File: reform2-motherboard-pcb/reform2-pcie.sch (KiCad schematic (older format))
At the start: 48 parts, among them J10 1-2199230-6, J11 48099-5701, Q14 PMV50EPEAR, U11 679105700, U23 IDT5V41066, Y3 25MHz

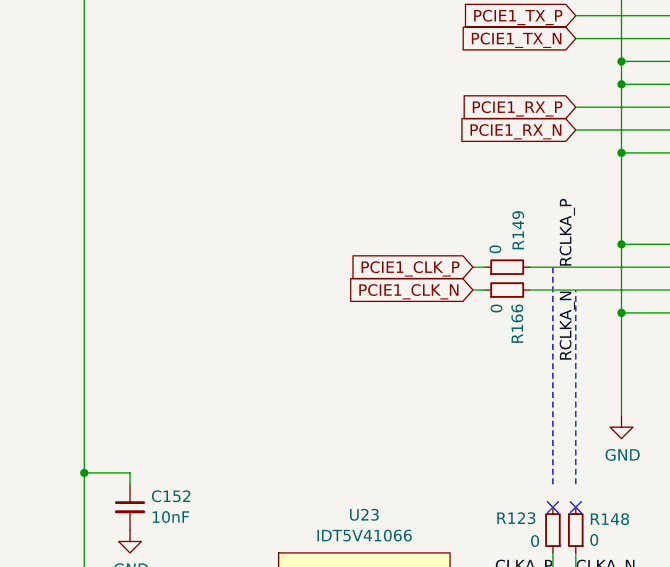
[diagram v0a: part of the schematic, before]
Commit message: WIP license clarification, motherboard now CERN-OHL-S 2.0
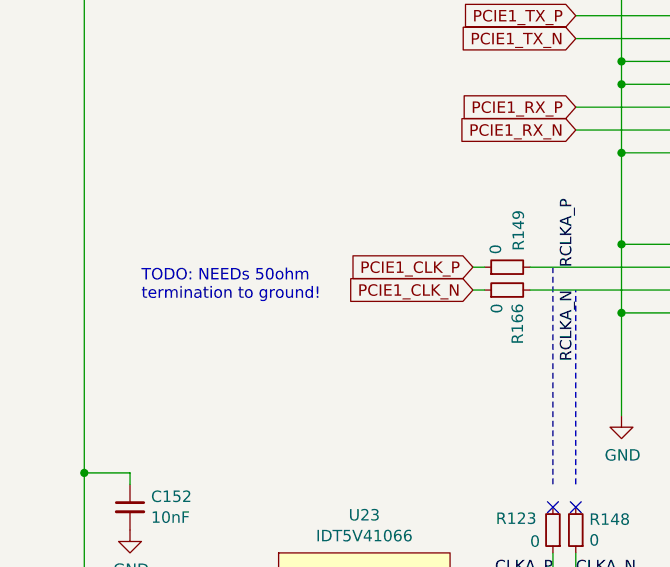
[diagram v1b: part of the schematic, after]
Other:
- note added: "TODO: NEEDs 50ohm\ntermination to ground!"
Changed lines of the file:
@@
 EESchema Schematic File Version 4
-LIBS:reform2-motherboard-cache
-EELAYER 29 0
+EELAYER 30 0
 EELAYER END
 $Descr A4 11693 8268
@@
 Sheet 5 9
 Title "MNT Reform 2 PCIe"
-Date "2020-02-07"
-Rev "2.0D-3"
+Date "2020-04-11"
+Rev "2.0D-4"
 Comp "MNT Research GmbH"
 Comment1 "https://mntre.com"
 Comment2 "Engineer: Lukas F. Hartmann"
-Comment3 "License: GPL v3+"
+Comment3 "License: CERN-OHL-S 2.0"
 Comment4 ""
 $EndDescr
@@
 $EndComp
 Connection ~ 7050 1800
-$Bitmap
-Pos 10600 6850
-Scale 1.000000
-Data
-89 50 4E 47 0D 0A 1A 0A 00 00 00 0D 49 48 44 52 00 00 01 2C 00 00 00 70 08 06 00 00 00 A4 46 4D
-4D 00 00 00 04 73 42 49 54 08 08 08 08 7C 08 64 88 00 00 06 2D 49 44 41 54 78 9C ED DD BB 8B 1D
-65 1C 87 F1 67 77 45 B1 08 82 26 F1 D2 6A 5A FF 00 0B B5 16 4C 36 12 5D 2F 9D 69 BC 04 0D 5E 62
-A3 A4 B1 D0 CE 4B C4 24 42 2A 05 03 21 85 FA 07 68 B4 8A 60 67 21 12 6D 04 0D 1A 90 04 4C 97 B5
-98 19 CE 64 F7 9C 39 B7 77 DE DF 7B F6 3C 1F 38 EC 16 CB EC 97 2D 1E 66 66 77 CF 80 24 49 92 24
-49 92 24 49 92 24 49 92 24 49 92 24 49 92 24 49 92 24 49 92 24 49 92 24 49 52 42 8F 00 7B A2 47
-B4 1C 8A 1E D0 F2 10 70 5F F4 08 49 03 C7 81 B3 94 13 AD 3F 80 67 A2 47 D4 8E 02 DF 60 B4 A4 62
-1C 07 36 29 27 5A D7 81 7F 28 23 5A 47 A9 7E 36 5F 63 B4 A4 22 34 C1 2A 25 5A D7 EB 2D 25 44 AB
-09 96 D1 92 0A D1 0E 56 09 D1 6A 82 55 42 B4 DA C1 32 5A 52 01 B6 06 AB 89 D6 EE A0 3D ED 60 45
-47 6B 6B B0 8C 96 14 6C 58 B0 22 A3 B5 35 58 91 D1 1A 16 2C A3 25 05 1A 15 AC A8 68 0D 0B 56 54
-B4 46 05 AB 89 D6 BD 99 F7 48 4B AF 2B 58 11 D1 1A 15 AC 88 68 75 05 6B 13 F8 0A A3 25 65 35 2E
-58 B9 A3 D5 15 AC 4D E0 6F F2 45 6B 5C B0 8C 96 94 D9 24 C1 DA 04 BE 24 4F B4 C6 05 2B 67 B4 26
-09 96 D1 92 32 9A 34 58 B9 A2 35 49 B0 9A 68 3D DD F3 96 49 83 65 B4 34 97 5B A2 07 EC 50 1B F5
-C7 23 54 F7 93 22 ED 06 3E 66 70 C9 1A ED 71 AA 2D 2F 00 7F F6 F4 3D 1E 05 6E ED E9 D8 7D B8 54
-BF 34 86 C1 EA 4F 69 D1 3A 51 7F 5E 42 B4 F6 D7 1F FB 8A D6 67 C4 FF 27 C2 34 DE AB 5F 1A C3 60
-F5 CB 68 8D D6 67 B4 76 01 77 24 3E 66 9F 6E 8B 1E B0 28 56 A3 07 2C 81 0D AA 50 44 FD 45 7C 5B
-13 AD 8D 71 5F 98 C9 7E E0 24 DE D3 D2 84 0C 56 1E 1B 54 F7 91 EE 8A 1E C2 E0 9E 96 D1 D2 C2 31
-58 F9 94 14 AD 3D 18 2D 2D 20 83 95 CF 0A D5 9F 17 18 AD E1 8C 96 C6 32 58 79 95 1A AD A7 A2 87
-D4 8C 96 3A 19 AC FC 4A 8C D6 09 8C 96 16 80 C1 8A 61 B4 BA ED 07 3E 05 EE 89 1E A2 B2 18 AC 38
-46 AB DB 01 E0 14 46 4B 2D 06 2B 96 D1 EA D6 5C 1E 1A 2D 01 06 AB 04 4D B4 3E C2 68 0D 73 80 EA
-F2 F0 EE E8 21 8A 67 B0 CA B0 42 F5 36 30 46 6B B8 75 AA 33 2D A3 B5 E4 0C 56 39 8C 56 37 A3 25
-83 55 98 52 A3 F5 64 F4 90 9A D1 5A 72 06 AB 3C A5 46 EB 50 F4 90 DA 3A DE D3 5A 5A 06 AB 4C A5
-45 6B 2F F0 09 E5 44 EB 20 46 6B 29 F9 7E 58 E5 6A A2 05 F0 0A 70 25 70 0B 0C A2 05 70 2E 72 48
-ED 60 FD F1 45 E0 72 0F C7 FF 17 F8 BC 87 E3 0E 73 31 D3 F7 D1 12 99 E6 3D DD 53 BE 6E 00 5F 00
-77 6E D9 33 E9 7B BA A7 7E 5D 66 FB 99 D6 34 EF E9 9E FA 75 9E ED 67 5A 7F 25 38 EE 2F A8 38 5E
-12 96 AF 7D 79 B8 35 5A 11 BC 3C 54 18 83 B5 18 56 80 67 81 0F 31 5A C3 18 AD 25 E1 3D AC C5 B1
-02 3C 57 7F FE 6A E4 90 5A FB 9E 56 09 DA F7 B4 B4 43 19 AC C5 D2 8E 56 09 67 C7 4D B4 7E 8C 1E
-52 6B A2 E5 43 1D 76 28 83 B5 78 DA D1 2A C1 5E E0 B1 E8 11 2D 07 A9 6E 9A 6B 07 32 58 8B 69 25
-7A C0 16 EE 51 16 25 5C 56 48 D2 44 0C 96 A4 85 61 B0 24 2D 0C 83 25 69 61 18 AC FC 4A FA 0D 56
-49 5B A0 BC 3D 2A 8C C1 CA EF 2C F0 5F F4 88 DA EF C0 B7 D1 23 5A CE 01 57 A3 47 A8 5C 06 2B BF
-33 C0 DB 94 11 AD 2B C0 61 CA 89 D6 59 E0 4D 8C 96 46 30 58 F9 DD A0 FA 9F C0 52 A2 F5 1B E5 44
-6B 13 38 8D D1 D2 08 06 2B 86 D1 EA 66 B4 34 94 C1 8A 63 B4 BA 19 2D 6D 63 B0 62 19 AD 6E 46 4B
-37 31 58 F1 8C 56 B7 D3 C0 31 8C 96 30 58 A5 30 5A DD 8C 96 00 83 55 92 52 A3 F5 5D F4 10 06 BF
-3D 3C 06 5C 0B DE A2 40 06 AB 2C 4D B4 DE A1 9C 68 3D 8F D1 52 21 0C 56 79 6E 00 1F 60 B4 86 D9
-04 4E 61 B4 96 96 C1 2A 93 D1 1A AD 89 D6 5B 18 AD A5 63 B0 CA 55 62 B4 0E 03 17 A2 87 50 45 EB
-24 46 6B E9 18 AC B2 95 16 AD 4B 54 67 5A 46 4B 21 7C 4F F7 C9 9D 07 7E 4D 70 9C 9F A7 FC FA 26
-5A 00 EF 02 B7 27 D8 30 8F 26 5A 67 80 87 83 B7 34 D1 02 78 1F D8 15 B8 45 52 CB 2A F0 1A D5 99
-56 AA C7 BC 5F 9C 63 CF FD 54 F7 B4 52 3E 76 FE 89 19 B7 AC 50 3D 8F F0 6A C2 2D 3E AA 5E 9A D3
-2A F0 3A E9 A2 35 4F B0 20 7D B4 66 0D 16 A4 8F 96 C1 92 12 58 05 DE 20 4D B4 E6 0D 16 C0 03 A4
-8B D6 3C C1 82 B4 D1 32 58 52 22 A9 A2 95 22 58 90 2E 5A F3 06 0B D2 45 CB 60 49 09 A5 88 56 AA
-60 41 9A 68 A5 08 16 A4 89 96 C1 92 12 9B 37 5A 29 83 05 55 B4 2E CC B8 25 65 B0 60 FE 68 19 2C
-A9 07 F3 44 2B 75 B0 60 BE 68 A5 0C 16 0C A2 75 6D 86 2D 06 4B EA C9 AC D1 EA 23 58 30 7B B4 52
-07 0B 66 8F 96 C1 92 7A 34 4B B4 FA 0A 16 CC 16 AD 3E 82 05 55 B4 5E 62 BA 68 19 2C A9 67 6B 4C
-17 AD 3E 83 05 D3 47 AB AF 60 C1 F4 D1 32 58 52 06 D3 44 AB EF 60 C1 74 D1 EA 33 58 50 45 EB 65
-26 8B 96 C1 92 32 99 34 5A 39 82 05 93 47 AB EF 60 C1 E4 D1 32 58 52 46 6B 54 4F 9C E9 8A 56 AE
-60 C1 64 D1 CA 11 2C 98 2C 5A 06 4B CA 6C 5C B4 72 06 0B AA 68 7D 3F 62 4B CE 60 C1 F8 68 19 2C
-29 40 57 B4 72 07 0B 60 1F A3 A3 95 33 58 D0 1D 2D 83 25 05 19 15 AD 88 60 C1 E8 68 E5 0E 16 8C
-8E 96 C1 92 02 0D 8B 56 54 B0 A0 8A D6 0F C4 07 0B 86 47 CB 60 49 C1 D6 A8 9E 38 73 9D F8 60 C1
-F6 68 45 05 0B AA 68 1D 61 10 2D 83 25 15 A0 1D AD E8 60 C1 CD D1 8A 0C 16 DC 1C 2D 83 25 15 A2
-89 56 09 0F 93 80 41 B4 A2 83 05 83 68 FD 14 3D 44 D2 C0 1A B0 1E 3D A2 65 1F F0 60 F4 88 DA 0A
-65 C4 53 92 24 49 92 24 49 92 24 49 92 24 49 92 24 49 92 24 49 92 24 49 92 24 49 92 24 49 52 41
-FE 07 39 BD 85 89 55 AA C4 B1 00 00 00 00 49 45 4E 44 AE 42 60 82
-EndData
-$EndBitmap
 Wire Wire Line
 	6350 5050 8200 5050
@@
 Wire Wire Line
 	6350 5050 6350 6200
+Text Notes 950  4350 0    50   ~ 0
+TODO: NEEDs 50ohm\ntermination to ground!
 $EndSCHEMATC

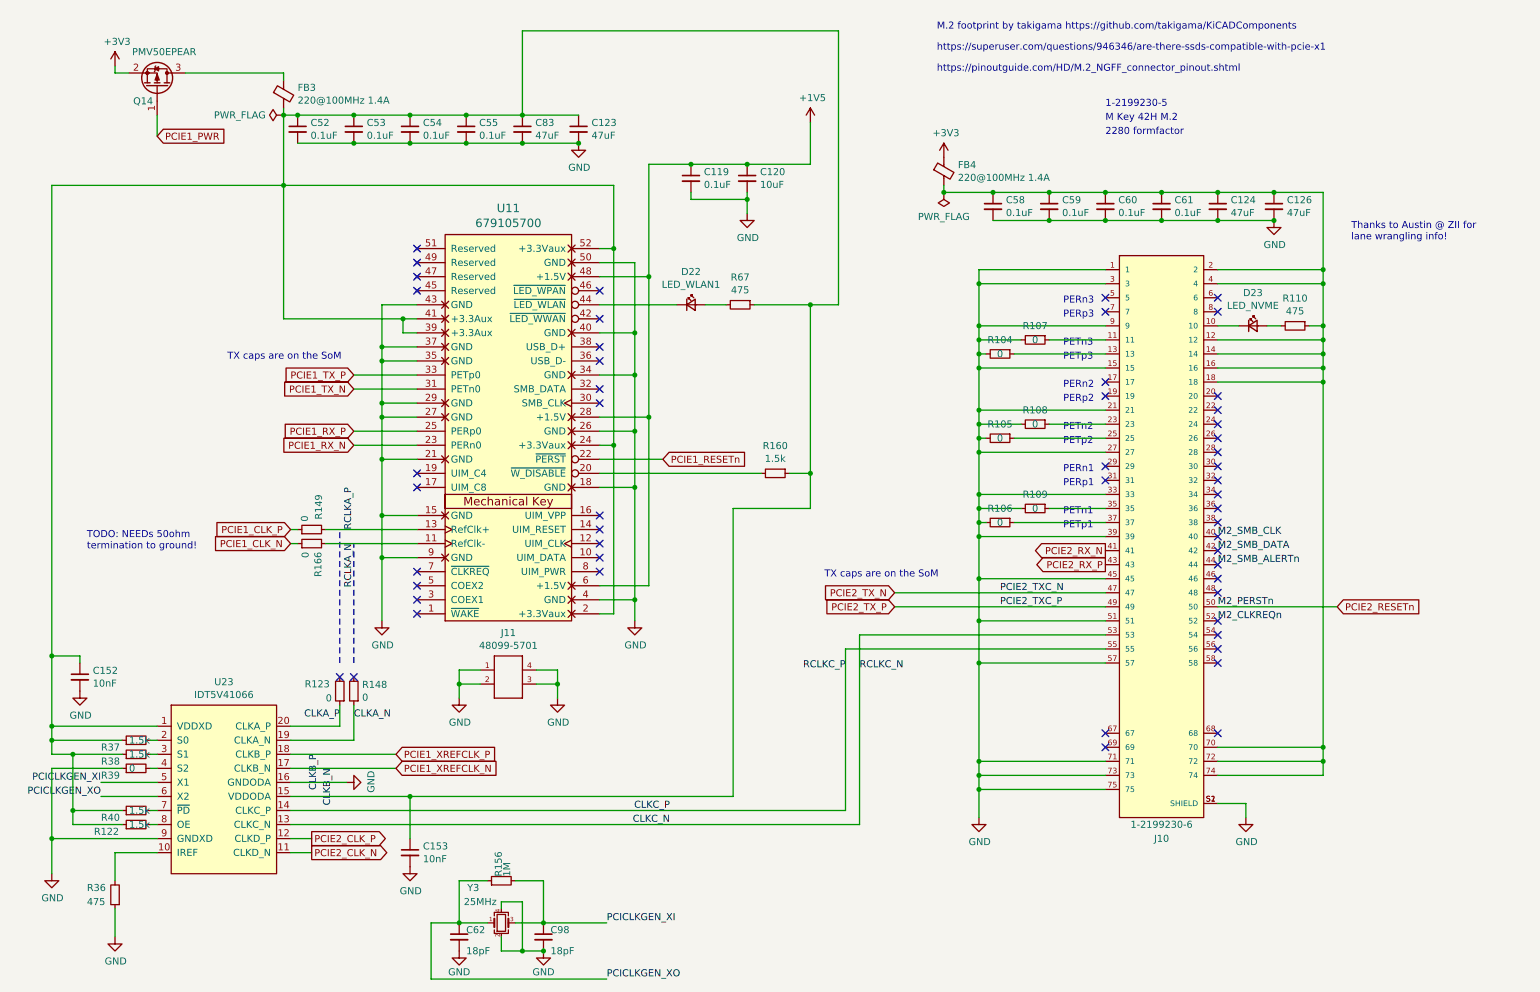
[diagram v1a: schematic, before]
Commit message: reform2-motherboard: version D-4 finished; fixes critical D-3 bugs; adds PCIe refclk termination, speaker output filter stage, pcie0 3v3 load switch, imx reset line to lpc, charge current control line to lpc
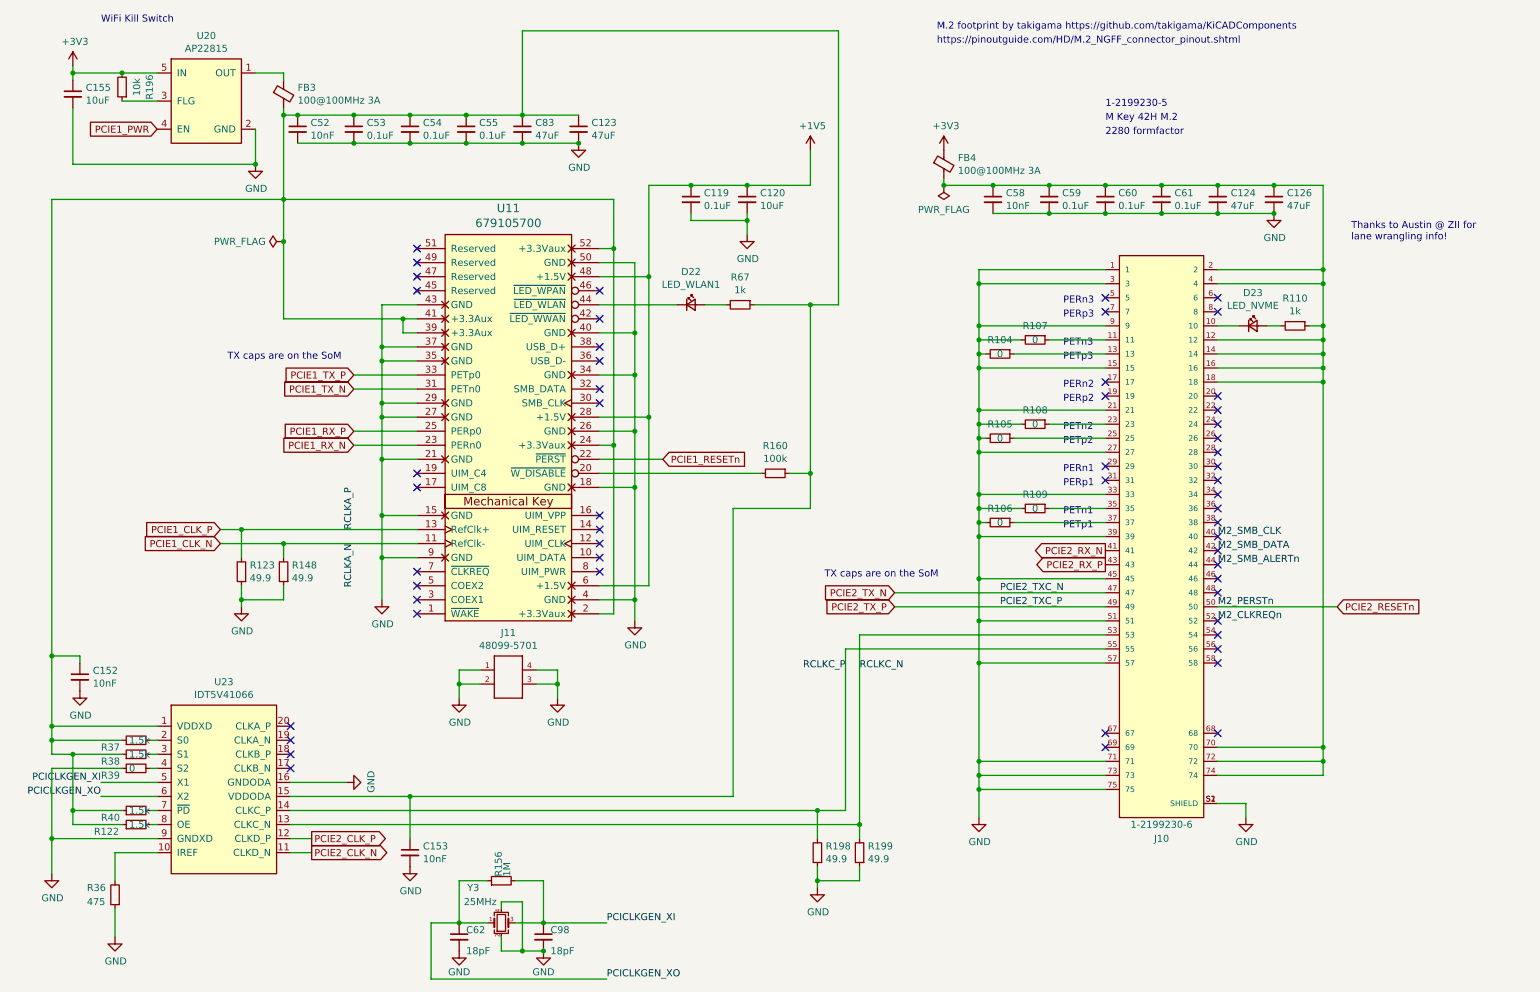
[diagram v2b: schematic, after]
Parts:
- removed Q14: PMV50EPEAR, Package_TO_SOT_SMD:SOT-23, symbol Transistor_FET:DMG2301L
- removed R149, R166: 0, Resistor_SMD:R_0603_1608Metric, symbol Device:R_Small
- added C155: 10uF, Capacitor_SMD:C_0603_1608Metric, symbol Device:C_Small
- added R196: 10k, Resistor_SMD:R_0603_1608Metric, symbol Device:R_Small
- added R198, R199: 49.9, Resistor_SMD:R_0603_1608Metric, symbol Device:R_Small
- added U20: AP22815, footprints:TSOT-25, symbol reform2:AP22815
- C52, C58: value 0.1uF -> 10nF; Manufacturer Yageo -> KEMET; Manufacturer_No CC0603JPX7R9BB104 -> C0603C103K5RAC3190
- FB3, FB4: value 220@100MHz 1.4A -> 100@100MHz 3A; Manufacturer_No BLM18PG221SH1D -> BLM18KG101TN1D
- R110, R67: value 475 -> 1k; Manufacturer_No RC0603FR-07475RL -> RC0603FR-071KL
- R123, R148: value 0 -> 49.9; Manufacturer Vishay Dale -> Yageo; Manufacturer_No CRCW06030000Z0EAC -> RC0603FR-1049R9L
- R160: value 1.5k -> 100k; Manufacturer Yageo -> Vishay Dale; Manufacturer_No RC0603FR-071K5L -> CRCW0603100KJNEAC
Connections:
- net RCLKA_N is gone; now on net PCIE1_CLK_N: U11.11 (RefClk-)
- net RCLKA_P is gone; now on net PCIE1_CLK_P: U11.13 (RefClk+)
- net +3V3: now also C155.1, R196.2, U20.5 (IN)
- net GND: now also R123.1, R148.1, C155.2, R198.1, R199.1, U20.2 (GND)
- net PCIE1_CLK_N: now also R148.2
- net PCIE1_CLK_P: now also R123.2
- net PCIE1_PWR: now also U20.4 (EN)
- net at FB3.1: now also U20.1 (OUT)
- net CLKA_N: no longer names the net of U23.19 (CLKA_N)
- net CLKA_N: no longer R148.1
- net CLKA_P: no longer names the net of U23.20 (CLKA_P)
- net CLKA_P: no longer R123.1
- net CLKC_N renamed RCLKC_N
- net RCLKC_N: now also R199.2
- net CLKC_P renamed RCLKC_P
- net RCLKC_P: now also R198.2
- net PCIE1_XREFCLK_N: no longer names the net of U23.17 (CLKB_N)
- net PCIE1_XREFCLK_P: no longer names the net of U23.18 (CLKB_P)
- new net: R196.1, U20.3 (FLG)
- no-connect marks 53 -> 55
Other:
- note added: "WiFi Kill Switch"
- note removed: "TODO: NEEDs 50ohm\ntermination to ground!"
- note removed: "https://superuser.com/questions/946346/are-there-ssds-compatible-with-pcie-x1"
- moved on the sheet: C119, C120, C124, C126, C58, C59, C60, C61, FB4

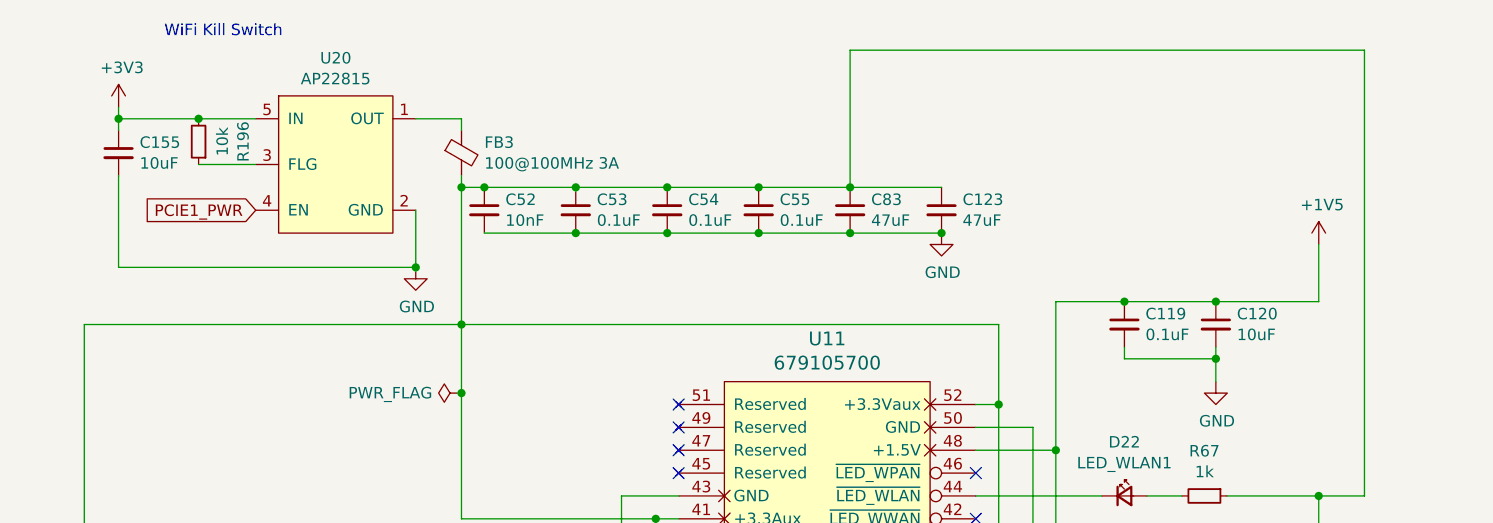
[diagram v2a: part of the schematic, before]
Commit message: reform2-motherboard: first R-1 snapshot. main changes: EMI, ESD, audio filter, enable FETs, SHDN fix, more rail switches
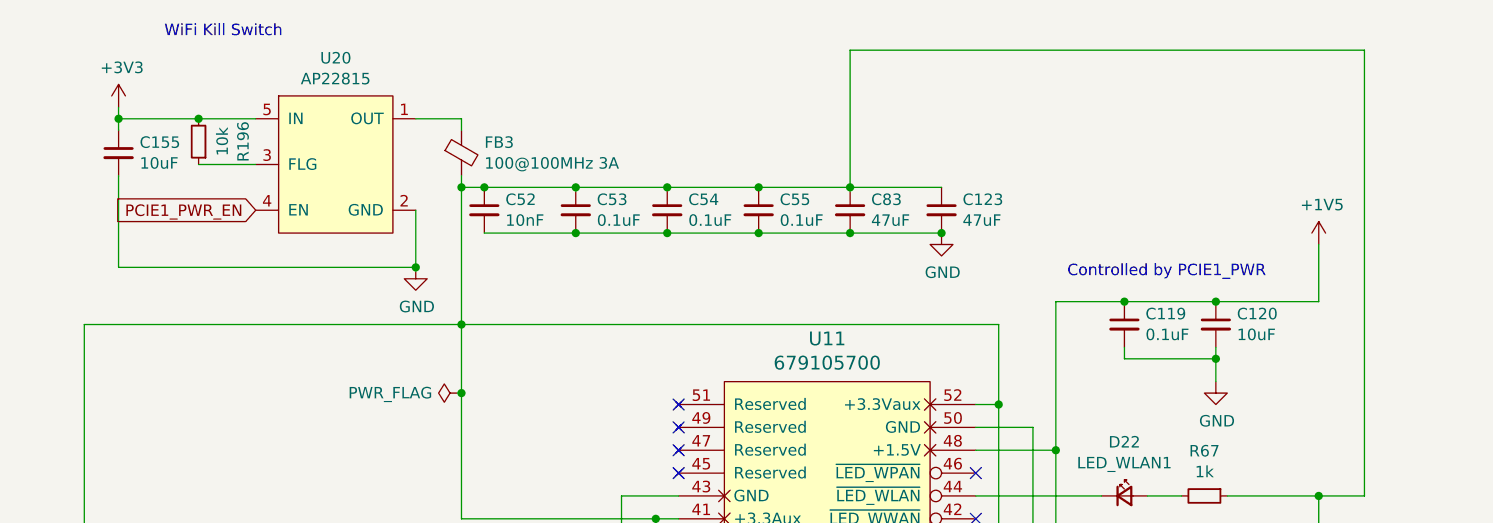
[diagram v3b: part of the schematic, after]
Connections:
- net PCIE1_PWR renamed PCIE1_PWR_EN
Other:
- note added: "Controlled by PCIE1_PWR"
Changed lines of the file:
@@
 $EndComp
 Text GLabel 1450 1350 0    50   Input ~ 0
-PCIE1_PWR
+PCIE1_PWR_EN
 Wire Wire Line
 	850  900  850  950
@@
 	1    0    0    -1
 $EndComp
+Text Notes 5000 1650 0    50   ~ 0
+Controlled by PCIE1_PWR
 $EndSCHEMATC

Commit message: motherboard: r-1 release snapshot
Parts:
- added R101: 0, Resistor_SMD:R_0603_1608Metric, symbol Device:R_Small
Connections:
- net at C123.1, C52.1, C53.1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: now also R101.2; no longer C152.1, C153.1, R122.1, R37.1, R38.1, R40.1, U23.1 (VDDXD), U23.15 (VDDODA)
- new net: C152.1, C153.1, R101.1, R122.1, R37.1, R38.1, R40.1, U23.1 (VDDXD), U23.15 (VDDODA)
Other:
- note added: "TODO: supply directly \nby AUX 3V3?"
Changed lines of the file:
@@
 Sheet 5 9
 Title "MNT Reform 2 PCIe"
-Date "2020-05-19"
-Rev "2.0D-4"
+Date "2020-09-24"
+Rev "2.0R-1"
 Comp "MNT Research GmbH"
 Comment1 "https://mntre.com"
@@
 	4050 650  4050 1250
 Wire Wire Line
-	5550 6100 5550 4050
-Wire Wire Line
-	5550 4050 6100 4050
-Wire Wire Line
-	6100 4050 6100 3800
-Connection ~ 6100 3800
-Wire Wire Line
 	6700 4750 8200 4750
 Wire Wire Line
@@
 	900  5100 900  5150
 Wire Wire Line
-	700  1850 700  5100
+	700  1850 700  4700
 Connection ~ 700  5100
 Wire Wire Line
@@
 Wire Wire Line
 	3250 6400 3250 6100
-Connection ~ 3250 6100
-Wire Wire Line
-	3250 6100 5550 6100
 $Comp
 L power:GND #PWR0215
@@
 Text Notes 5000 1650 0    50   ~ 0
 Controlled by PCIE1_PWR
+Wire Wire Line
+	3250 6100 3250 5000
+Wire Wire Line
+	3250 5000 1750 5000
+Connection ~ 3250 6100
+Connection ~ 700  5000
+Wire Wire Line
+	700  5000 700  5100
+$Comp
+L Device:R_Small R101
+U 1 1 5FF52117
+P 700 4800
+F 0 "R101" V 600 4800 50  0000 C CNN
+F 1 "0" V 700 4800 50  0000 C CNN
+F 2 "Resistor_SMD:R_0603_1608Metric" H 700 4800 50  0001 C CNN
+F 3 "~" H 700 4800 50  0001 C CNN
+F 4 "Vishay Dale" H 700 4800 50  0001 C CNN "Manufacturer"
+F 5 "CRCW06030000Z0EAC" H 700 4800 50  0001 C CNN "Manufacturer_No"
+F 6 "Mouser" H 700 4800 50  0001 C CNN "Distributor"
+F 7 "y" H 700 4800 50  0001 C CNN "Checked"
+	1    700  4800
+	-1   0    0    1
+$EndComp
+Wire Wire Line
+	700  4900 700  5000
+Text Notes 850  4850 0    50   ~ 0
+TODO: supply directly \nby AUX 3V3?
+$Comp
+L power:PWR_FLAG #FLG0114
+U 1 1 5FF63199
+P 1750 5000
+F 0 "#FLG0114" H 1750 5075 50  0001 C CNN
+F 1 "PWR_FLAG" V 1750 5127 50  0000 L CNN
+F 2 "" H 1750 5000 50  0001 C CNN
+F 3 "~" H 1750 5000 50  0001 C CNN
+	1    1750 5000
+	1    0    0    -1
+$EndComp
+Connection ~ 1750 5000
+Wire Wire Line
+	1750 5000 700  5000
 $EndSCHEMATC
